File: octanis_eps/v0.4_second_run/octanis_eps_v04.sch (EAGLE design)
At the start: 101 parts, among them IC1 OPA2333DGK, IC5 OPA2333DGK, IC7 OPA2333DGK, IC9 OPA2333DGK, Q1 FC-12M, Q2 N-HEXFET-2D_SOT232-, Q3 N-HEXFET-2D_SOT232-, Q4 N-HEXFET-2D_SOT232-

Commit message: various corrections on EPS v0.3, new v0.4 for second run
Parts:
- removed A_EXT: (no value), jumper:JP4E
- removed R37: 50m, rcl:R-EU_R1206
- added BT_CHG, DSP_CMD: (no value), pinhead:PINHD-1X1
- added JP2: (no value), jumper:JP4Q
- added U$9: 50m, Octanis1_EPS:CURRENT_RESISTOR
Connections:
- new net N$38: R38.1, U$9.I2
- new net N$40: R39.1, U$9.I1
- net A_EXT1: now also JP2.7; no longer A_EXT.4
- net A_EXT2: now also JP2.5; no longer A_EXT.3
- net A_EXT3: now also JP2.3; no longer A_EXT.2
- net A_EXT4: now also JP2.1; no longer A_EXT.1
- net BT+: now also U$9.V1; no longer R37.1, R39.1
- net BT_CHG: now also BT_CHG.1, U$9.V2; no longer R37.2, R38.1
- net GND: now also JP2.2, JP2.4, JP2.6, JP2.8
- net N$45: now also DSP_CMD.1

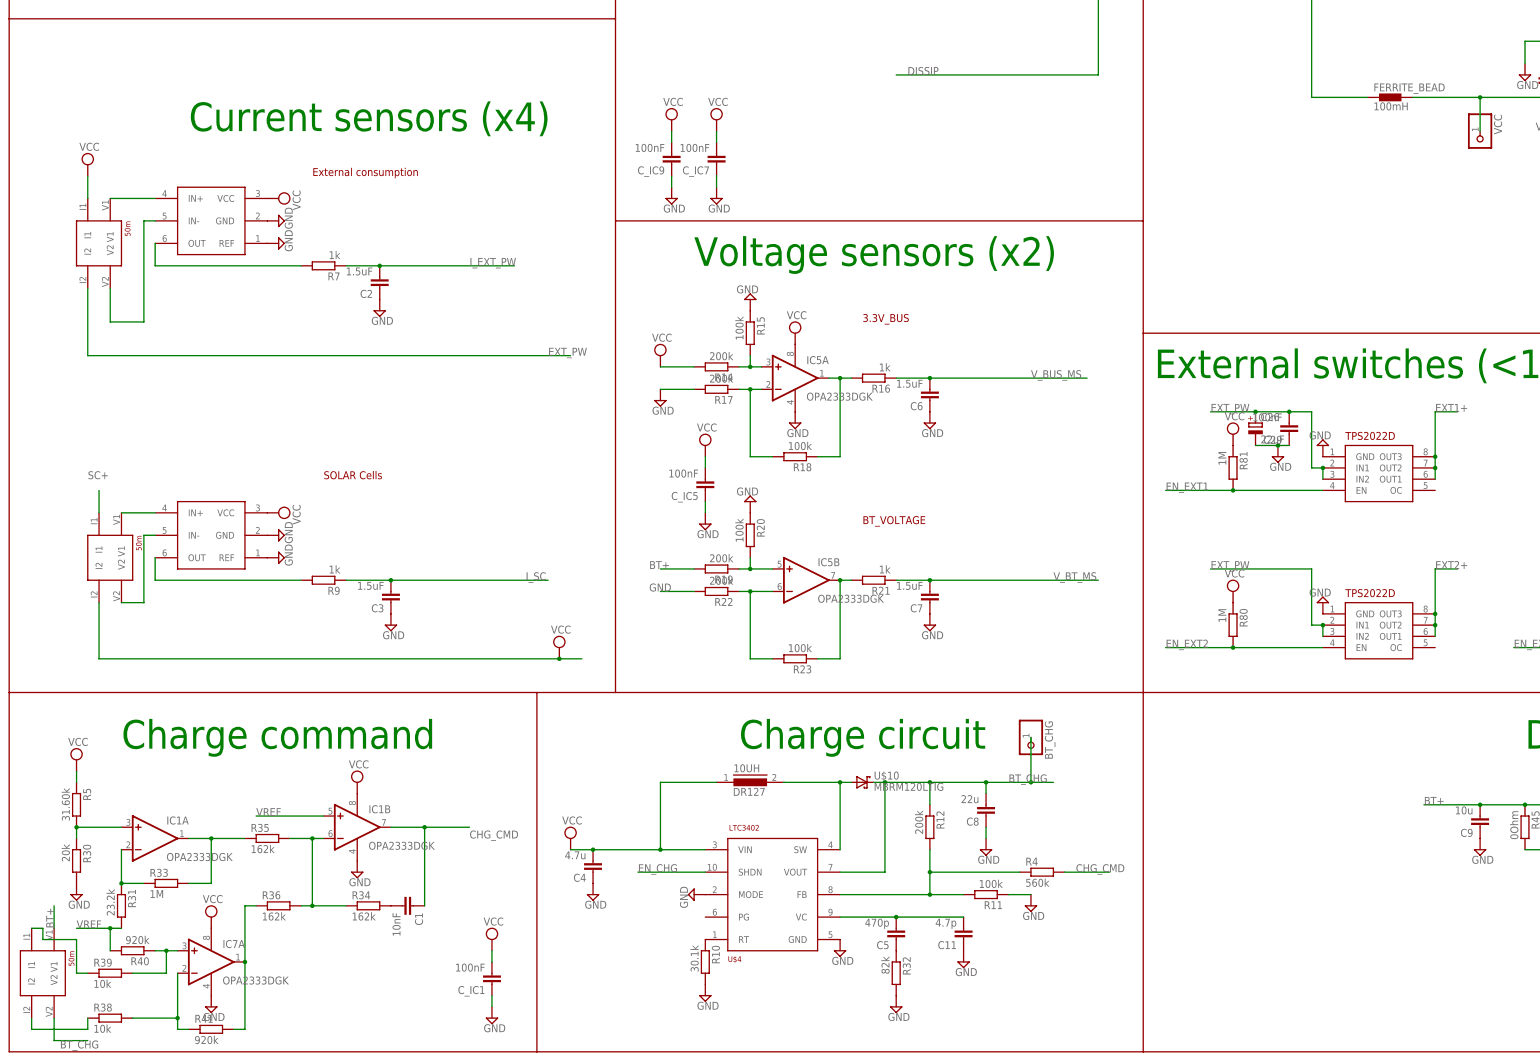
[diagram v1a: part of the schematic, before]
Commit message: modified silk screen for EPS
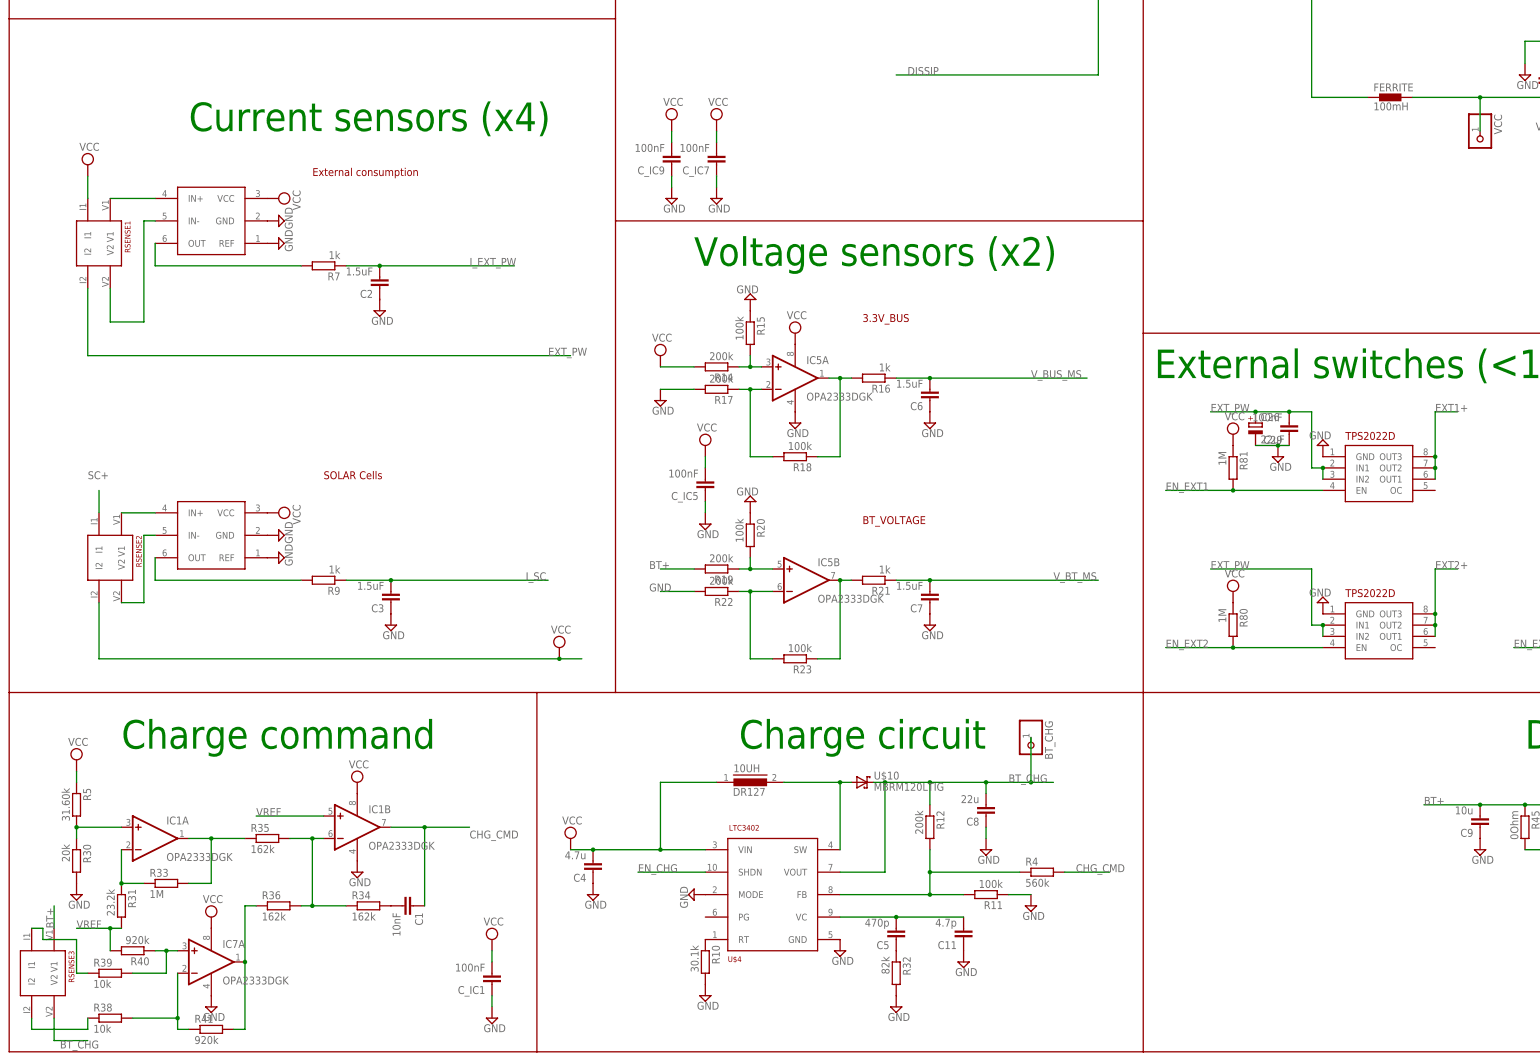
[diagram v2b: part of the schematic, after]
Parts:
- RSENSE2: value 50m -> RSENSE2
- RSENSE3: value 50m -> RSENSE3
- R_SENSE1: value 50m -> RSENSE1
- renumbered FERRITE_BEAD to FERRITE, U$1 to R_SENSE1, U$8 to RSENSE2, U$9 to RSENSE3
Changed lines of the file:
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@@
 <part name="C22" library="rcl" deviceset="C-EU" device="C0603" value="100nF"/>
 <part name="C24" library="rcl" deviceset="CPOL-EU" device="A/3216-18R" value="10uF"/>
-<part name="FERRITE_BEAD" library="inductors" deviceset="BLM15H" device="" technology="D601SN1" value="100mH"/>
+<part name="FERRITE" library="inductors" deviceset="BLM15H" device="" technology="D601SN1" value="100mH"/>
 <part name="C26" library="rcl" deviceset="CPOL-EU" device="A/3216-18R" value="22uF"/>
 <part name="C29" library="rcl" deviceset="C-EU" device="C0603" value="100nF"/>
@@
 <part name="SUPPLY55" library="supply2" deviceset="VCC" device=""/>
 <part name="SUPPLY56" library="supply2" deviceset="VCC" device=""/>
-<part name="U$1" library="Octanis1_EPS" deviceset="CURRENT_RESISTOR" device="" value="50m"/>
-<part name="U$8" library="Octanis1_EPS" deviceset="CURRENT_RESISTOR" device="" value="50m"/>
-<part name="U$9" library="Octanis1_EPS" deviceset="CURRENT_RESISTOR" device="" value="50m"/>
+<part name="R_SENSE1" library="Octanis1_EPS" deviceset="CURRENT_RESISTOR" device="" value="RSENSE1"/>
+<part name="RSENSE2" library="Octanis1_EPS" deviceset="CURRENT_RESISTOR" device="" value="RSENSE2"/>
+<part name="RSENSE3" library="Octanis1_EPS" deviceset="CURRENT_RESISTOR" device="" value="RSENSE3"/>
 <part name="BT_CHG" library="pinhead" deviceset="PINHD-1X1" device=""/>
 <part name="DSP_CMD" library="pinhead" deviceset="PINHD-1X1" device=""/>
@@
 <instance part="C22" gate="G$1" x="256.54" y="38.1"/>
 <instance part="C24" gate="G$1" x="266.7" y="38.1"/>
-<instance part="FERRITE_BEAD" gate="G$1" x="269.24" y="-2.54"/>
+<instance part="FERRITE" gate="G$1" x="269.24" y="-2.54"/>
 <instance part="C26" gate="G$1" x="238.76" y="-76.2"/>
 <instance part="C29" gate="G$1" x="246.38" y="-78.74" rot="R180"/>
@@
 <instance part="SUPPLY55" gate="G$1" x="261.62" y="45.72"/>
 <instance part="SUPPLY56" gate="G$1" x="266.7" y="50.8"/>
-<instance part="U$1" gate="G$1" x="-22.86" y="-40.64" rot="R270"/>
-<instance part="U$8" gate="G$1" x="-20.32" y="-111.76" rot="R270"/>
-<instance part="U$9" gate="G$1" x="-35.56" y="-205.74" rot="R270"/>
+<instance part="R_SENSE1" gate="G$1" x="-22.86" y="-40.64" rot="R270"/>
+<instance part="RSENSE2" gate="G$1" x="-20.32" y="-111.76" rot="R270"/>
+<instance part="RSENSE3" gate="G$1" x="-35.56" y="-205.74" rot="R270"/>
 <instance part="BT_CHG" gate="G$1" x="187.96" y="-149.86" rot="R270"/>
 <instance part="DSP_CMD" gate="G$1" x="185.42" y="58.42" rot="R270"/>
@@
 <wire x1="81.28" y1="-129.54" x2="86.36" y2="-129.54" width="0.1524" layer="91"/>
 <junction x="81.28" y="-129.54"/>
-<pinref part="U$8" gate="G$1" pin="I2"/>
+<pinref part="RSENSE2" gate="G$1" pin="I2"/>
 </segment>
 <segment>
@@
 <segment>
 <pinref part="SUPPLY119" gate="G$1" pin="VCC"/>
-<pinref part="U$1" gate="G$1" pin="I1"/>
+<pinref part="R_SENSE1" gate="G$1" pin="I1"/>
 <wire x1="-25.4" y1="-20.32" x2="-25.4" y2="-25.4" width="0.1524" layer="91"/>
 </segment>
@@
 <pinref part="C21" gate="G$1" pin="2"/>
 <junction x="304.8" y="-2.54"/>
-<pinref part="FERRITE_BEAD" gate="G$1" pin="2"/>
+<pinref part="FERRITE" gate="G$1" pin="2"/>
 <wire x1="304.8" y1="-2.54" x2="289.56" y2="-2.54" width="0.1524" layer="91"/>
 <pinref part="VCC" gate="G$1" pin="1"/>
@@
 <pinref part="U$6" gate="G$1" pin="DVCC"/>
 <wire x1="330.2" y1="43.18" x2="266.7" y2="43.18" width="0.1524" layer="91"/>
-<pinref part="FERRITE_BEAD" gate="G$1" pin="1"/>
+<pinref part="FERRITE" gate="G$1" pin="1"/>
 <wire x1="264.16" y1="-2.54" x2="251.46" y2="-2.54" width="0.1524" layer="91"/>
 <wire x1="251.46" y1="-2.54" x2="251.46" y2="43.18" width="0.1524" layer="91"/>
@@
 <wire x1="-22.86" y1="-96.52" x2="-22.86" y2="-91.44" width="0.1524" layer="91"/>
 <label x="-25.4" y="-88.9" size="1.778" layer="95"/>
-<pinref part="U$8" gate="G$1" pin="I1"/>
+<pinref part="RSENSE2" gate="G$1" pin="I1"/>
 </segment>
 <segment>
@@
 <segment>
 <label x="-33.02" y="-190.5" size="1.778" layer="95" rot="R90"/>
-<pinref part="U$9" gate="G$1" pin="V1"/>
+<pinref part="RSENSE3" gate="G$1" pin="V1"/>
 <wire x1="-33.02" y1="-185.42" x2="-33.02" y2="-190.5" width="0.1524" layer="91"/>
 </segment>
@@
 <wire x1="-25.4" y1="-45.72" x2="-25.4" y2="-60.96" width="0.1524" layer="91"/>
 <label x="78.74" y="-60.96" size="1.778" layer="95"/>
-<pinref part="U$1" gate="G$1" pin="I2"/>
+<pinref part="R_SENSE1" gate="G$1" pin="I2"/>
 </segment>
 <segment>
@@
 <label x="-22.86" y="-215.9" size="1.778" layer="95" rot="R180"/>
 <wire x1="-25.4" y1="-215.9" x2="-33.02" y2="-215.9" width="0.1524" layer="91"/>
-<pinref part="U$9" gate="G$1" pin="V2"/>
+<pinref part="RSENSE3" gate="G$1" pin="V2"/>
 <wire x1="-33.02" y1="-210.82" x2="-33.02" y2="-215.9" width="0.1524" layer="91"/>
 </segment>
@@
 <wire x1="-20.32" y1="-25.4" x2="-10.16" y2="-25.4" width="0.1524" layer="91"/>
 <pinref part="U$2" gate="G$1" pin="IN+"/>
-<pinref part="U$1" gate="G$1" pin="V1"/>
+<pinref part="R_SENSE1" gate="G$1" pin="V1"/>
 </segment>
 </net>
 <net name="N$33" class="0">
 <segment>
-<pinref part="U$1" gate="G$1" pin="V2"/>
+<pinref part="R_SENSE1" gate="G$1" pin="V2"/>
 <wire x1="-20.32" y1="-45.72" x2="-20.32" y2="-53.34" width="0.1524" layer="91"/>
 <wire x1="-20.32" y1="-53.34" x2="-12.7" y2="-53.34" width="0.1524" layer="91"/>
@@
 <net name="N$34" class="0">
 <segment>
-<pinref part="U$8" gate="G$1" pin="V1"/>
+<pinref part="RSENSE2" gate="G$1" pin="V1"/>
 <pinref part="U$3" gate="G$1" pin="IN+"/>
 <wire x1="-17.78" y1="-96.52" x2="-10.16" y2="-96.52" width="0.1524" layer="91"/>
@@
 <net name="N$35" class="0">
 <segment>
-<pinref part="U$8" gate="G$1" pin="V2"/>
+<pinref part="RSENSE2" gate="G$1" pin="V2"/>
 <wire x1="-17.78" y1="-116.84" x2="-12.7" y2="-116.84" width="0.1524" layer="91"/>
 <wire x1="-12.7" y1="-116.84" x2="-12.7" y2="-101.6" width="0.1524" layer="91"/>
@@
 <wire x1="-25.4" y1="-213.36" x2="-25.4" y2="-210.82" width="0.1524" layer="91"/>
 <pinref part="R38" gate="G$1" pin="1"/>
-<pinref part="U$9" gate="G$1" pin="I2"/>
+<pinref part="RSENSE3" gate="G$1" pin="I2"/>
 <wire x1="-38.1" y1="-210.82" x2="-38.1" y2="-213.36" width="0.1524" layer="91"/>
 <wire x1="-38.1" y1="-213.36" x2="-25.4" y2="-213.36" width="0.1524" layer="91"/>
@@
 <wire x1="-25.4" y1="-200.66" x2="-27.94" y2="-200.66" width="0.1524" layer="91"/>
 <wire x1="-27.94" y1="-200.66" x2="-27.94" y2="-193.04" width="0.1524" layer="91"/>
-<pinref part="U$9" gate="G$1" pin="I1"/>
+<pinref part="RSENSE3" gate="G$1" pin="I1"/>
 <wire x1="-38.1" y1="-190.5" x2="-35.56" y2="-190.5" width="0.1524" layer="91"/>
 <wire x1="-35.56" y1="-190.5" x2="-35.56" y2="-193.04" width="0.1524" layer="91"/>

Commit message: added pull down on boost Cvtr enable pin, C1 and R34 in parallel, Note that Rsense = 10 mOhms instead of 50mOhms at the entry of the INA213 current sensors, Rsense 3 still at 50mOhms
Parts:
- added R6: 100k, rcl:R-EU_R0603
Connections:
- removed net N$27: C1.2, R34.2
- net CHG_CMD: now also R34.2
- net EN_CHG: now also R6.1
- net GND: now also R6.2
- net N$11: now also C1.2
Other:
- note added: "Vref=1.25V"
- note removed: "Vref"
- moved on the sheet: C1
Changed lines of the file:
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@@
 <part name="JP2" library="jumper" deviceset="JP4Q" device=""/>
 <part name="SUPPLY57" library="supply2" deviceset="GND" device=""/>
+<part name="R6" library="rcl" deviceset="R-EU_" device="R0603" value="100k"/>
+<part name="SUPPLY59" library="supply2" deviceset="GND" device=""/>
 </parts>
 <sheets>
@@
 <wire x1="-43.18" y1="15.24" x2="-43.18" y2="101.6" width="0.1524" layer="94"/>
 <wire x1="-43.18" y1="101.6" x2="93.98" y2="101.6" width="0.1524" layer="94"/>
-<text x="396.24" y="-66.04" size="6.4516" layer="91">Vref</text>
+<text x="383.54" y="-66.04" size="6.4516" layer="91">Vref=1.25V</text>
 <text x="-2.54" y="-10.16" size="6.4516" layer="91">Current sensors (x4)</text>
 <wire x1="93.98" y1="15.24" x2="93.98" y2="-30.48" width="0.1524" layer="94"/>
@@
 <instance part="R35" gate="G$1" x="15.24" y="-170.18"/>
 <instance part="R36" gate="G$1" x="17.78" y="-185.42"/>
-<instance part="C1" gate="G$1" x="48.26" y="-185.42" rot="R270"/>
+<instance part="C1" gate="G$1" x="40.64" y="-190.5" rot="R270"/>
 <instance part="SUPPLY48" gate="G$1" x="35.56" y="-157.48"/>
 <instance part="SUPPLY49" gate="GND" x="35.56" y="-177.8"/>
@@
 <instance part="JP2" gate="B" x="347.98" y="81.28" rot="R270"/>
 <instance part="SUPPLY57" gate="GND" x="360.68" y="73.66"/>
+<instance part="R6" gate="G$1" x="101.6" y="-182.88" rot="R270"/>
+<instance part="SUPPLY59" gate="GND" x="101.6" y="-190.5"/>
 </instances>
 <busses>
@@
 <junction x="360.68" y="81.28"/>
 </segment>
+<segment>
+<pinref part="R6" gate="G$1" pin="2"/>
+<pinref part="SUPPLY59" gate="GND" pin="GND"/>
+</segment>
 </net>
 <net name="VCC" class="0">
@@
 <segment>
 <pinref part="U$4" gate="G$1" pin="SHDN"/>
-<wire x1="114.3" y1="-177.8" x2="99.06" y2="-177.8" width="0.1524" layer="91"/>
+<wire x1="114.3" y1="-177.8" x2="101.6" y2="-177.8" width="0.1524" layer="91"/>
 <label x="99.06" y="-177.8" size="1.778" layer="95"/>
+<pinref part="R6" gate="G$1" pin="1"/>
+<wire x1="101.6" y1="-177.8" x2="99.06" y2="-177.8" width="0.1524" layer="91"/>
+<junction x="101.6" y="-177.8"/>
 </segment>
 <segment>
@@
 </segment>
 <segment>
+<pinref part="IC1" gate="B" pin="OUT"/>
+<wire x1="43.18" y1="-167.64" x2="50.8" y2="-167.64" width="0.1524" layer="91"/>
+<label x="60.96" y="-170.18" size="1.778" layer="95"/>
 <pinref part="C1" gate="G$1" pin="1"/>
+<pinref part="R34" gate="G$1" pin="2"/>
+<wire x1="50.8" y1="-167.64" x2="60.96" y2="-167.64" width="0.1524" layer="91"/>
+<wire x1="43.18" y1="-190.5" x2="43.18" y2="-185.42" width="0.1524" layer="91"/>
+<wire x1="43.18" y1="-185.42" x2="50.8" y2="-185.42" width="0.1524" layer="91"/>
 <wire x1="50.8" y1="-185.42" x2="50.8" y2="-167.64" width="0.1524" layer="91"/>
-<pinref part="IC1" gate="B" pin="OUT"/>
-<wire x1="50.8" y1="-167.64" x2="43.18" y2="-167.64" width="0.1524" layer="91"/>
-<wire x1="50.8" y1="-167.64" x2="60.96" y2="-167.64" width="0.1524" layer="91"/>
+<junction x="43.18" y="-185.42"/>
 <junction x="50.8" y="-167.64"/>
-<label x="60.96" y="-170.18" size="1.778" layer="95"/>
 </segment>
 </net>
@@
 <pinref part="R36" gate="G$1" pin="2"/>
 <wire x1="25.4" y1="-170.18" x2="27.94" y2="-170.18" width="0.1524" layer="91"/>
-<wire x1="33.02" y1="-185.42" x2="25.4" y2="-185.42" width="0.1524" layer="91"/>
+<wire x1="33.02" y1="-185.42" x2="30.48" y2="-185.42" width="0.1524" layer="91"/>
+<wire x1="30.48" y1="-185.42" x2="25.4" y2="-185.42" width="0.1524" layer="91"/>
 <wire x1="25.4" y1="-185.42" x2="22.86" y2="-185.42" width="0.1524" layer="91"/>
 <wire x1="25.4" y1="-170.18" x2="25.4" y2="-185.42" width="0.1524" layer="91"/>
 <junction x="25.4" y="-170.18"/>
 <junction x="25.4" y="-185.42"/>
-</segment>
-</net>
-<net name="N$27" class="0">
-<segment>
-<pinref part="R34" gate="G$1" pin="2"/>
 <pinref part="C1" gate="G$1" pin="2"/>
-</segment>
-</net>
+<wire x1="35.56" y1="-190.5" x2="30.48" y2="-190.5" width="0.1524" layer="91"/>
+<wire x1="30.48" y1="-190.5" x2="30.48" y2="-185.42" width="0.1524" layer="91"/>
+<junction x="30.48" y="-185.42"/>
+</segment>
+</net>
